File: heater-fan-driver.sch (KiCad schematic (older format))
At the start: 35 parts

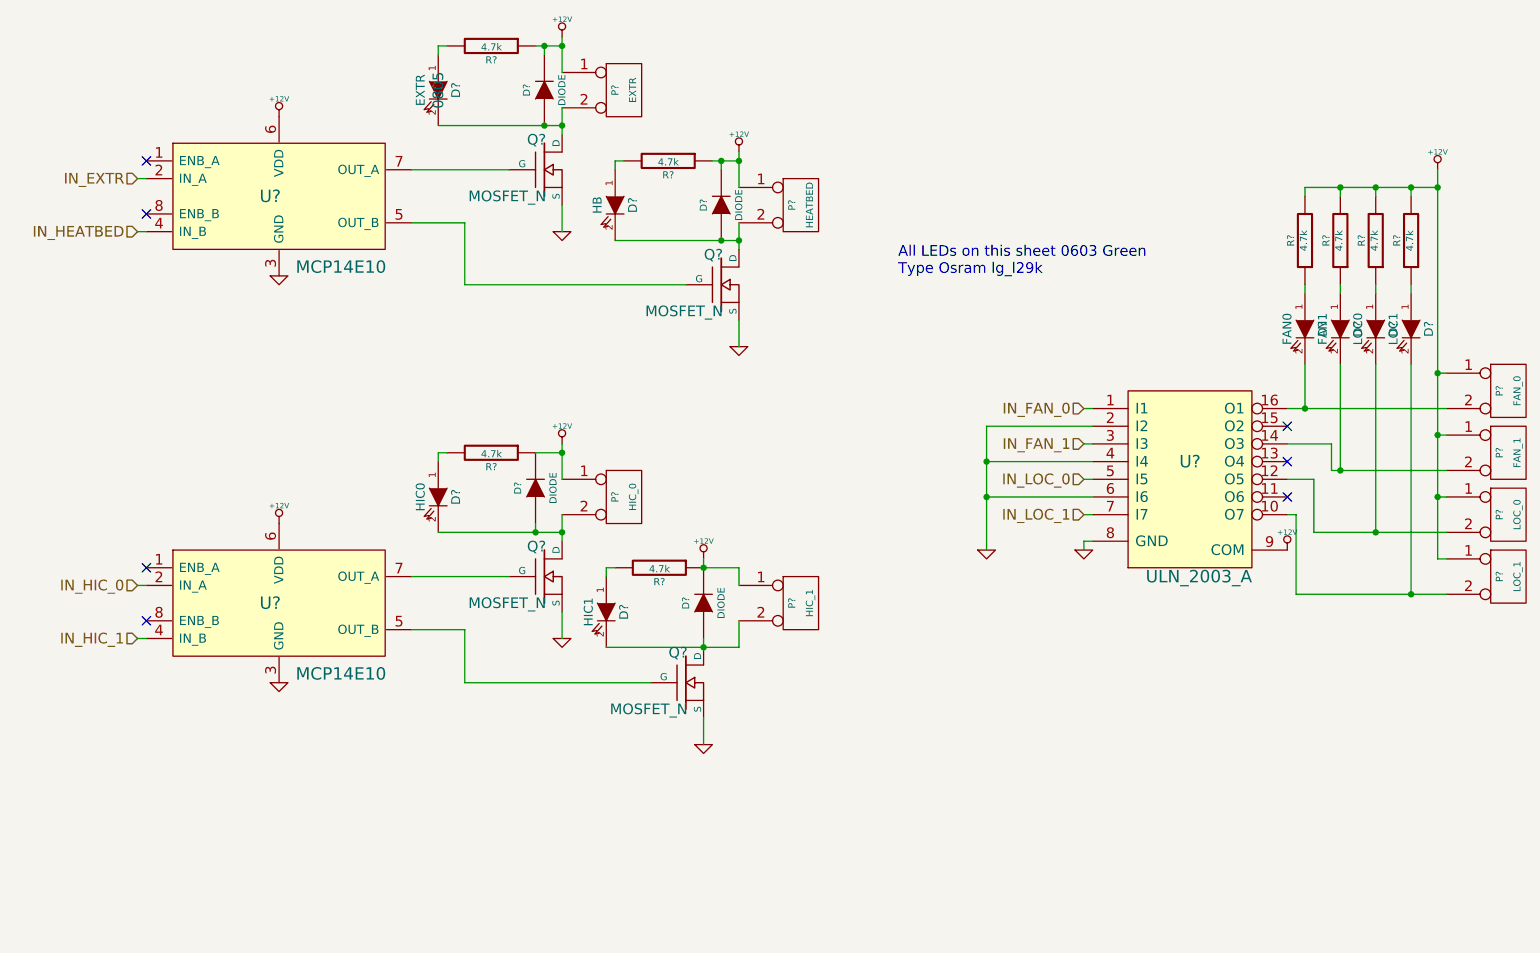
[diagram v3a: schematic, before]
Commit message: Added some LEDs for a better overview what the board is doing when operating; Generated netlist and started to associate footprints
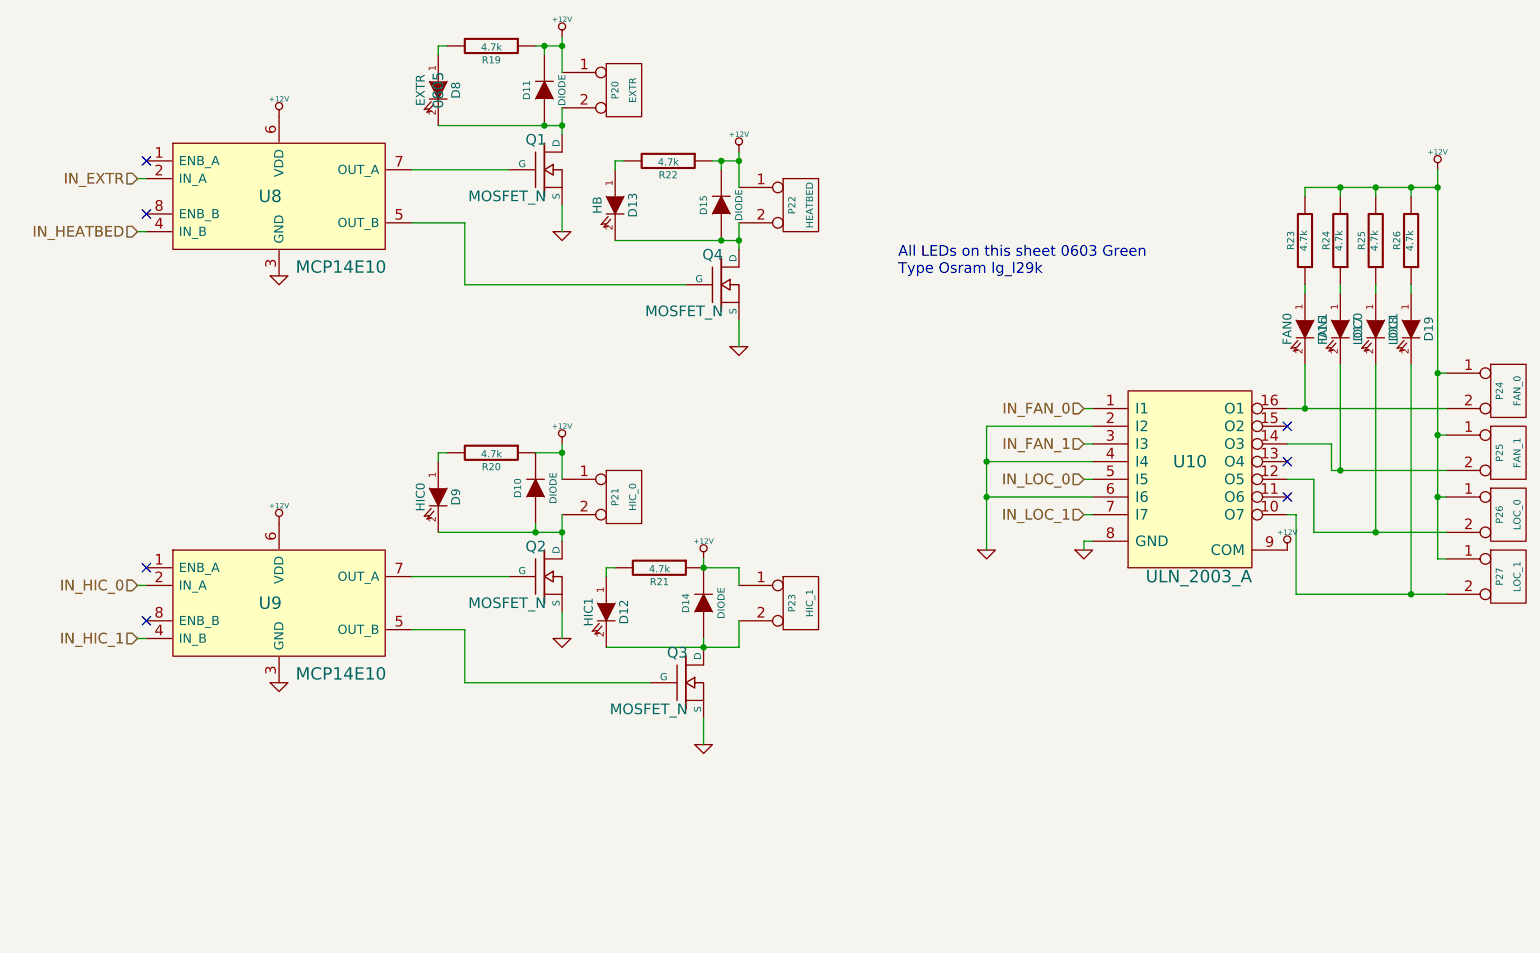
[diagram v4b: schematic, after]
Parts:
- D12, D13, D16, D17, D18, D19, D8, D9: renamed from D?; Color (none) -> Green
- gave numbers to parts that had none: 27

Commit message: Added decoupling cap for display supply; Associated most footprints.
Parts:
- renumbered R19 to R23, R20 to R24, R21 to R25, R22 to R26, R23 to R27, R24 to R28, R25 to R29, R26 to R30
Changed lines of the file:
@@
 NoConn ~ 1500 3100
 $Comp
-L +12V #PWR081
+L +12V #PWR83
 U 1 1 534EA91F
 P 2250 2550
-F 0 "#PWR081" H 2250 2500 20  0001 C CNN
+F 0 "#PWR83" H 2250 2500 20  0001 C CNN
 F 1 "+12V" H 2250 2650 30  0000 C CNN
 F 2 "" H 2250 2550 60  0000 C CNN
@@
 $EndComp
 $Comp
-L GND #PWR082
+L GND #PWR84
 U 1 1 534EA925
 P 2250 3450
-F 0 "#PWR082" H 2250 3450 30  0001 C CNN
+F 0 "#PWR84" H 2250 3450 30  0001 C CNN
 F 1 "GND" H 2250 3380 30  0001 C CNN
 F 2 "" H 2250 3450 60  0000 C CNN
@@
 NoConn ~ 1500 5400
 $Comp
-L +12V #PWR083
+L +12V #PWR85
 U 1 1 534EA949
 P 2250 4850
-F 0 "#PWR083" H 2250 4800 20  0001 C CNN
+F 0 "#PWR85" H 2250 4800 20  0001 C CNN
 F 1 "+12V" H 2250 4950 30  0000 C CNN
 F 2 "" H 2250 4850 60  0000 C CNN
@@
 $EndComp
 $Comp
-L GND #PWR084
+L GND #PWR86
 U 1 1 534EA94F
 P 2250 5750
-F 0 "#PWR084" H 2250 5750 30  0001 C CNN
+F 0 "#PWR86" H 2250 5750 30  0001 C CNN
 F 1 "GND" H 2250 5680 30  0001 C CNN
 F 2 "" H 2250 5750 60  0000 C CNN
@@
 $EndComp
 $Comp
-L GND #PWR085
+L GND #PWR88
 U 1 1 534EC0D7
 P 3850 3200
-F 0 "#PWR085" H 3850 3200 30  0001 C CNN
+F 0 "#PWR88" H 3850 3200 30  0001 C CNN
 F 1 "GND" H 3850 3130 30  0001 C CNN
 F 2 "" H 3850 3200 60  0000 C CNN
@@
 	3850 2500 3850 2650
 $Comp
-L +12V #PWR086
+L +12V #PWR87
 U 1 1 534EC0F8
 P 3850 2100
-F 0 "#PWR086" H 3850 2050 20  0001 C CNN
+F 0 "#PWR87" H 3850 2050 20  0001 C CNN
 F 1 "+12V" H 3850 2200 30  0000 C CNN
 F 2 "" H 3850 2100 60  0000 C CNN
@@
 $EndComp
 $Comp
-L GND #PWR087
+L GND #PWR94
 U 1 1 534EC131
 P 4850 3850
-F 0 "#PWR087" H 4850 3850 30  0001 C CNN
+F 0 "#PWR94" H 4850 3850 30  0001 C CNN
 F 1 "GND" H 4850 3780 30  0001 C CNN
 F 2 "" H 4850 3850 60  0000 C CNN
@@
 	4850 3150 4850 3300
 $Comp
-L +12V #PWR088
+L +12V #PWR93
 U 1 1 534EC139
 P 4850 2750
-F 0 "#PWR088" H 4850 2700 20  0001 C CNN
+F 0 "#PWR93" H 4850 2700 20  0001 C CNN
 F 1 "+12V" H 4850 2850 30  0000 C CNN
 F 2 "" H 4850 2750 60  0000 C CNN
@@
 $EndComp
 $Comp
-L GND #PWR089
+L GND #PWR90
 U 1 1 534EC15C
 P 3850 5500
-F 0 "#PWR089" H 3850 5500 30  0001 C CNN
+F 0 "#PWR90" H 3850 5500 30  0001 C CNN
 F 1 "GND" H 3850 5430 30  0001 C CNN
 F 2 "" H 3850 5500 60  0000 C CNN
@@
 	3850 4800 3850 4950
 $Comp
-L +12V #PWR090
+L +12V #PWR89
 U 1 1 534EC164
 P 3850 4400
-F 0 "#PWR090" H 3850 4350 20  0001 C CNN
+F 0 "#PWR89" H 3850 4350 20  0001 C CNN
 F 1 "+12V" H 3850 4500 30  0000 C CNN
 F 2 "" H 3850 4400 60  0000 C CNN
@@
 $EndComp
 $Comp
-L GND #PWR091
+L GND #PWR92
 U 1 1 534EC178
 P 4650 6100
-F 0 "#PWR091" H 4650 6100 30  0001 C CNN
+F 0 "#PWR92" H 4650 6100 30  0001 C CNN
 F 1 "GND" H 4650 6030 30  0001 C CNN
 F 2 "" H 4650 6100 60  0000 C CNN
@@
 	4650 6100 4650 5950
 $Comp
-L +12V #PWR092
+L +12V #PWR91
 U 1 1 534EC180
 P 4650 5050
-F 0 "#PWR092" H 4650 5000 20  0001 C CNN
+F 0 "#PWR91" H 4650 5000 20  0001 C CNN
 F 1 "+12V" H 4650 5150 30  0000 C CNN
 F 2 "" H 4650 5050 60  0000 C CNN
@@
 $EndComp
 $Comp
-L GND #PWR093
+L GND #PWR96
 U 1 1 534EF1D5
 P 6800 5000
-F 0 "#PWR093" H 6800 5000 30  0001 C CNN
+F 0 "#PWR96" H 6800 5000 30  0001 C CNN
 F 1 "GND" H 6800 4930 30  0001 C CNN
 F 2 "" H 6800 5000 60  0000 C CNN
@@
 	6800 4950 6850 4950
 $Comp
-L +12V #PWR094
+L +12V #PWR97
 U 1 1 534EF1FB
 P 7950 5000
-F 0 "#PWR094" H 7950 4950 20  0001 C CNN
+F 0 "#PWR97" H 7950 4950 20  0001 C CNN
 F 1 "+12V" H 7950 5100 30  0000 C CNN
 F 2 "" H 7950 5000 60  0000 C CNN
@@
 	6800 4800 6850 4800
 $Comp
-L GND #PWR095
+L GND #PWR95
 U 1 1 534EF2C3
 P 6250 5000
-F 0 "#PWR095" H 6250 5000 30  0001 C CNN
+F 0 "#PWR95" H 6250 5000 30  0001 C CNN
 F 1 "GND" H 6250 4930 30  0001 C CNN
 F 2 "" H 6250 5000 60  0000 C CNN
@@
 $EndComp
 $Comp
-L +12V #PWR096
+L +12V #PWR98
 U 1 1 534EF366
 P 8800 2850
-F 0 "#PWR096" H 8800 2800 20  0001 C CNN
+F 0 "#PWR98" H 8800 2800 20  0001 C CNN
 F 1 "+12V" H 8800 2950 30  0000 C CNN
 F 2 "" H 8800 2850 60  0000 C CNN
@@
 $EndComp
 $Comp
-L R R19
+L R R23
 U 1 1 53500760
 P 3450 2150
-F 0 "R19" V 3530 2150 40  0000 C CNN
+F 0 "R23" V 3530 2150 40  0000 C CNN
 F 1 "4.7k" V 3457 2151 40  0000 C CNN
 F 2 "" V 3380 2150 30  0000 C CNN
@@
 $EndComp
 $Comp
-L R R22
+L R R26
 U 1 1 535007F7
 P 4450 2800
-F 0 "R22" V 4530 2800 40  0000 C CNN
+F 0 "R26" V 4530 2800 40  0000 C CNN
 F 1 "4.7k" V 4457 2801 40  0000 C CNN
 F 2 "" V 4380 2800 30  0000 C CNN
@@
 $EndComp
 $Comp
-L R R20
+L R R24
 U 1 1 535008E5
 P 3450 4450
-F 0 "R20" V 3530 4450 40  0000 C CNN
+F 0 "R24" V 3530 4450 40  0000 C CNN
 F 1 "4.7k" V 3457 4451 40  0000 C CNN
 F 2 "" V 3380 4450 30  0000 C CNN
@@
 $EndComp
 $Comp
-L R R21
+L R R25
 U 1 1 535008FD
 P 4400 5100
-F 0 "R21" V 4480 5100 40  0000 C CNN
+F 0 "R25" V 4480 5100 40  0000 C CNN
 F 1 "4.7k" V 4407 5101 40  0000 C CNN
 F 2 "" V 4330 5100 30  0000 C CNN
@@
 Connection ~ 8250 2950
 $Comp
-L R R23
+L R R27
 U 1 1 53500AE3
 P 8050 3250
-F 0 "R23" V 8130 3250 40  0000 C CNN
+F 0 "R27" V 8130 3250 40  0000 C CNN
 F 1 "4.7k" V 8057 3251 40  0000 C CNN
 F 2 "" V 7980 3250 30  0000 C CNN
@@
 	8800 2850 8800 5050
 $Comp
-L R R24
+L R R28
 U 1 1 53500D59
 P 8250 3250
-F 0 "R24" V 8330 3250 40  0000 C CNN
+F 0 "R28" V 8330 3250 40  0000 C CNN
 F 1 "4.7k" V 8257 3251 40  0000 C CNN
 F 2 "" V 8180 3250 30  0000 C CNN
@@
 $EndComp
 $Comp
-L R R25
+L R R29
 U 1 1 53500D64
 P 8450 3250
-F 0 "R25" V 8530 3250 40  0000 C CNN
+F 0 "R29" V 8530 3250 40  0000 C CNN
 F 1 "4.7k" V 8457 3251 40  0000 C CNN
 F 2 "" V 8380 3250 30  0000 C CNN
@@
 $EndComp
 $Comp
-L R R26
+L R R30
 U 1 1 53500D6F
 P 8650 3250
-F 0 "R26" V 8730 3250 40  0000 C CNN
+F 0 "R30" V 8730 3250 40  0000 C CNN
 F 1 "4.7k" V 8657 3251 40  0000 C CNN
 F 2 "" V 8580 3250 30  0000 C CNN

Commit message: Finished footprint association; added footprint for potentiometer
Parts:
- Q1, Q2, Q3, Q4: value MOSFET_N -> IRL1404
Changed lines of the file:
@@
 NoConn ~ 1500 3100
 $Comp
-L +12V #PWR83
+L +12V #PWR083
 U 1 1 534EA91F
 P 2250 2550
-F 0 "#PWR83" H 2250 2500 20  0001 C CNN
+F 0 "#PWR083" H 2250 2500 20  0001 C CNN
 F 1 "+12V" H 2250 2650 30  0000 C CNN
 F 2 "" H 2250 2550 60  0000 C CNN
@@
 $EndComp
 $Comp
-L GND #PWR84
+L GND #PWR084
 U 1 1 534EA925
 P 2250 3450
-F 0 "#PWR84" H 2250 3450 30  0001 C CNN
+F 0 "#PWR084" H 2250 3450 30  0001 C CNN
 F 1 "GND" H 2250 3380 30  0001 C CNN
 F 2 "" H 2250 3450 60  0000 C CNN
@@
 NoConn ~ 1500 5400
 $Comp
-L +12V #PWR85
+L +12V #PWR085
 U 1 1 534EA949
 P 2250 4850
-F 0 "#PWR85" H 2250 4800 20  0001 C CNN
+F 0 "#PWR085" H 2250 4800 20  0001 C CNN
 F 1 "+12V" H 2250 4950 30  0000 C CNN
 F 2 "" H 2250 4850 60  0000 C CNN
@@
 $EndComp
 $Comp
-L GND #PWR86
+L GND #PWR086
 U 1 1 534EA94F
 P 2250 5750
-F 0 "#PWR86" H 2250 5750 30  0001 C CNN
+F 0 "#PWR086" H 2250 5750 30  0001 C CNN
 F 1 "GND" H 2250 5680 30  0001 C CNN
 F 2 "" H 2250 5750 60  0000 C CNN
@@
 P 3750 2850
 F 0 "Q1" H 3760 3020 60  0000 R CNN
-F 1 "MOSFET_N" H 3760 2700 60  0000 R CNN
+F 1 "IRL1404" H 3760 2700 60  0000 R CNN
 F 2 "" H 3750 2850 60  0000 C CNN
 F 3 "" H 3750 2850 60  0000 C CNN
@@
 $EndComp
 $Comp
-L GND #PWR88
+L GND #PWR087
 U 1 1 534EC0D7
 P 3850 3200
-F 0 "#PWR88" H 3850 3200 30  0001 C CNN
+F 0 "#PWR087" H 3850 3200 30  0001 C CNN
 F 1 "GND" H 3850 3130 30  0001 C CNN
 F 2 "" H 3850 3200 60  0000 C CNN
@@
 	3850 2500 3850 2650
 $Comp
-L +12V #PWR87
+L +12V #PWR088
 U 1 1 534EC0F8
 P 3850 2100
-F 0 "#PWR87" H 3850 2050 20  0001 C CNN
+F 0 "#PWR088" H 3850 2050 20  0001 C CNN
 F 1 "+12V" H 3850 2200 30  0000 C CNN
 F 2 "" H 3850 2100 60  0000 C CNN
@@
 P 4750 3500
 F 0 "Q4" H 4760 3670 60  0000 R CNN
-F 1 "MOSFET_N" H 4760 3350 60  0000 R CNN
+F 1 "IRL1404" H 4760 3350 60  0000 R CNN
 F 2 "" H 4750 3500 60  0000 C CNN
 F 3 "" H 4750 3500 60  0000 C CNN
@@
 $EndComp
 $Comp
-L GND #PWR94
+L GND #PWR089
 U 1 1 534EC131
 P 4850 3850
-F 0 "#PWR94" H 4850 3850 30  0001 C CNN
+F 0 "#PWR089" H 4850 3850 30  0001 C CNN
 F 1 "GND" H 4850 3780 30  0001 C CNN
 F 2 "" H 4850 3850 60  0000 C CNN
@@
 	4850 3150 4850 3300
 $Comp
-L +12V #PWR93
+L +12V #PWR090
 U 1 1 534EC139
 P 4850 2750
-F 0 "#PWR93" H 4850 2700 20  0001 C CNN
+F 0 "#PWR090" H 4850 2700 20  0001 C CNN
 F 1 "+12V" H 4850 2850 30  0000 C CNN
 F 2 "" H 4850 2750 60  0000 C CNN
@@
 P 3750 5150
 F 0 "Q2" H 3760 5320 60  0000 R CNN
-F 1 "MOSFET_N" H 3760 5000 60  0000 R CNN
+F 1 "IRL1404" H 3760 5000 60  0000 R CNN
 F 2 "" H 3750 5150 60  0000 C CNN
 F 3 "" H 3750 5150 60  0000 C CNN
@@
 $EndComp
 $Comp
-L GND #PWR90
+L GND #PWR091
 U 1 1 534EC15C
 P 3850 5500
-F 0 "#PWR90" H 3850 5500 30  0001 C CNN
+F 0 "#PWR091" H 3850 5500 30  0001 C CNN
 F 1 "GND" H 3850 5430 30  0001 C CNN
 F 2 "" H 3850 5500 60  0000 C CNN
@@
 	3850 4800 3850 4950
 $Comp
-L +12V #PWR89
+L +12V #PWR092
 U 1 1 534EC164
 P 3850 4400
-F 0 "#PWR89" H 3850 4350 20  0001 C CNN
+F 0 "#PWR092" H 3850 4350 20  0001 C CNN
 F 1 "+12V" H 3850 4500 30  0000 C CNN
 F 2 "" H 3850 4400 60  0000 C CNN
@@
 P 4550 5750
 F 0 "Q3" H 4560 5920 60  0000 R CNN
-F 1 "MOSFET_N" H 4560 5600 60  0000 R CNN
+F 1 "IRL1404" H 4560 5600 60  0000 R CNN
 F 2 "" H 4550 5750 60  0000 C CNN
 F 3 "" H 4550 5750 60  0000 C CNN
@@
 $EndComp
 $Comp
-L GND #PWR92
+L GND #PWR093
 U 1 1 534EC178
 P 4650 6100
-F 0 "#PWR92" H 4650 6100 30  0001 C CNN
+F 0 "#PWR093" H 4650 6100 30  0001 C CNN
 F 1 "GND" H 4650 6030 30  0001 C CNN
 F 2 "" H 4650 6100 60  0000 C CNN
@@
 	4650 6100 4650 5950
 $Comp
-L +12V #PWR91
+L +12V #PWR094
 U 1 1 534EC180
 P 4650 5050
-F 0 "#PWR91" H 4650 5000 20  0001 C CNN
+F 0 "#PWR094" H 4650 5000 20  0001 C CNN
 F 1 "+12V" H 4650 5150 30  0000 C CNN
 F 2 "" H 4650 5050 60  0000 C CNN
@@
 $EndComp
 $Comp
-L GND #PWR96
+L GND #PWR095
 U 1 1 534EF1D5
 P 6800 5000
-F 0 "#PWR96" H 6800 5000 30  0001 C CNN
+F 0 "#PWR095" H 6800 5000 30  0001 C CNN
 F 1 "GND" H 6800 4930 30  0001 C CNN
 F 2 "" H 6800 5000 60  0000 C CNN
@@
 	6800 4950 6850 4950
 $Comp
-L +12V #PWR97
+L +12V #PWR096
 U 1 1 534EF1FB
 P 7950 5000
-F 0 "#PWR97" H 7950 4950 20  0001 C CNN
+F 0 "#PWR096" H 7950 4950 20  0001 C CNN
 F 1 "+12V" H 7950 5100 30  0000 C CNN
 F 2 "" H 7950 5000 60  0000 C CNN
@@
 	6800 4800 6850 4800
 $Comp
-L GND #PWR95
+L GND #PWR097
 U 1 1 534EF2C3
 P 6250 5000
-F 0 "#PWR95" H 6250 5000 30  0001 C CNN
+F 0 "#PWR097" H 6250 5000 30  0001 C CNN
 F 1 "GND" H 6250 4930 30  0001 C CNN
 F 2 "" H 6250 5000 60  0000 C CNN
@@
 $EndComp
 $Comp
-L +12V #PWR98
+L +12V #PWR098
 U 1 1 534EF366
 P 8800 2850
-F 0 "#PWR98" H 8800 2800 20  0001 C CNN
+F 0 "#PWR098" H 8800 2800 20  0001 C CNN
 F 1 "+12V" H 8800 2950 30  0000 C CNN
 F 2 "" H 8800 2850 60  0000 C CNN
